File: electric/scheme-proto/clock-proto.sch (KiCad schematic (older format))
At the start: 134 parts, among them K1 servo, K2 1-wire, P1 batt, P10 led, P11 p2, P12 btn-4, P13 led, P14 led, P15 btn-5, P2 speaker, P3 dist, P4 btn-1, P5 btn-2, P6 btn-3, P7 led, P8 p1, P9 p3, Q1 bc857, Q10 bc847, Q11 bc847, Q12 bc857, Q13 bc857, Q14 bc847, Q15 bc847, Q16 bc847, Q17 bc857, Q18 bc857, Q2 bc847, Q3 bc857, Q4 bc847, Q5 irlml2244, Q6 bc847, Q7 bc857, Q8 bc847, Q9 bc857, U1 3310-LCD, U2 AD8607_2, U3 SD, U4 MINI-USB-B, U5 AD8607_2, U6 NCP3063, U7 NCP3063, U8 DS18S20

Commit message: Designing the circuit.
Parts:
- added unit 2 of U5
- U1: footprint (none) -> ~
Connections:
- net labels added: amp-vdd, nc1, nc2
- net labels removed: nc
- wire segments 431 -> 439
- no-connect marks 33 -> 34
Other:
- note added: "This is unused OpAmp part."
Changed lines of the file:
@@
 Sheet 1 1
 Title ""
-Date "18 feb 2014"
+Date "21 feb 2014"
 Rev ""
 Comp ""
@@
 	8700 3750 8700 4600
 Connection ~ 8700 4600
-Wire Wire Line
-	9800 6500 9800 6700
 $Comp
 L GND #PWR07
@@
 	1    0    0    -1
 $EndComp
-Wire Wire Line
-	8550 7100 8550 7300
 $Comp
 L GND #PWR09
@@
 Wire Wire Line
 	8900 7200 8550 7200
-Connection ~ 8550 7200
 Connection ~ 6300 13050
 Wire Wire Line
@@
 	20100 20250 20400 20250
 Wire Wire Line
-	19300 20350 19300 20550
+	19300 20200 19300 20550
 Wire Wire Line
 	20150 22200 20150 22450
@@
 $EndComp
 $Comp
-L 3310-LCD U1
-U 1 1 5301199A
-P 2150 20550
-F 0 "U1" H 2100 20650 60  0000 C CNN
-F 1 "3310-LCD" H 2050 20500 60  0000 C CNN
-F 2 "" H 2150 20550 60  0001 C CNN
-F 3 "" H 2150 20550 60  0001 C CNN
-	1    2150 20550
-	1    0    0    -1
-$EndComp
-$Comp
 L GND #PWR028
 U 1 1 53011AB9
@@
 gnd
 Text Label 28600 17600 0    60   ~ 0
-nc
+nc1
 Text Label 28600 17700 0    60   ~ 0
 3v3
@@
 gnd
 Text Label 31000 17600 0    60   ~ 0
-nc
+nc2
 Text Label 31000 17700 0    60   ~ 0
 5v
@@
 NoConn ~ 31250 17800
 $Comp
-L PWR_FLAG #FLG?
+L PWR_FLAG #FLG080
 U 1 1 5304928D
 P 8950 16500
-F 0 "#FLG?" H 8950 16595 30  0001 C CNN
+F 0 "#FLG080" H 8950 16595 30  0001 C CNN
 F 1 "PWR_FLAG" H 8950 16680 30  0000 C CNN
 F 2 "" H 8950 16500 60  0000 C CNN
@@
 	8950 16500 8950 16650
 Connection ~ 8950 16650
+$Comp
+L 3310-LCD U1
+U 1 1 5306E2C6
+P 2150 20550
+F 0 "U1" H 2100 20650 60  0000 C CNN
+F 1 "3310-LCD" H 2050 20500 60  0000 C CNN
+F 2 "~" H 2150 20550 60  0000 C CNN
+F 3 "~" H 2150 20550 60  0000 C CNN
+	1    2150 20550
+	1    0    0    -1
+$EndComp
+$Comp
+L PWR_FLAG #FLG081
+U 1 1 5306E441
+P 19300 20200
+F 0 "#FLG081" H 19300 20295 30  0001 C CNN
+F 1 "PWR_FLAG" H 19300 20380 30  0000 C CNN
+F 2 "" H 19300 20200 60  0000 C CNN
+F 3 "" H 19300 20200 60  0000 C CNN
+	1    19300 20200
+	1    0    0    -1
+$EndComp
+Wire Wire Line
+	8550 7100 8550 7300
+Connection ~ 8550 7200
+Wire Wire Line
+	9800 6700 9800 6500
+$Comp
+L PWR_FLAG #FLG082
+U 1 1 5306FE63
+P 10050 6400
+F 0 "#FLG082" H 10050 6495 30  0001 C CNN
+F 1 "PWR_FLAG" H 10050 6580 30  0000 C CNN
+F 2 "" H 10050 6400 60  0000 C CNN
+F 3 "" H 10050 6400 60  0000 C CNN
+	1    10050 6400
+	1    0    0    -1
+$EndComp
+Wire Wire Line
+	10050 6400 10050 6600
+Wire Wire Line
+	10050 6600 9800 6600
+Connection ~ 9800 6600
+$Comp
+L AD8607_2 U5
+U 2 1 530703A8
+P 15850 8500
+F 0 "U5" H 15650 8450 30  0000 C CNN
+F 1 "AD8607_2" H 15650 8550 30  0000 C CNN
+F 2 "~" H 15950 8500 60  0000 C CNN
+F 3 "~" H 15950 8500 60  0000 C CNN
+	2    15850 8500
+	1    0    0    -1
+$EndComp
+Wire Wire Line
+	14550 8300 15150 8300
+Text Label 16100 2750 0    60   ~ 0
+amp-vdd
+Text Label 15900 7800 0    60   ~ 0
+amp-vdd
+Wire Wire Line
+	15850 8000 15850 7800
+Wire Wire Line
+	15850 7800 16350 7800
+Wire Wire Line
+	15850 9000 15850 9200
+$Comp
+L GND #PWR083
+U 1 1 53070C1B
+P 15850 9200
+F 0 "#PWR083" H 15850 9200 30  0001 C CNN
+F 1 "GND" H 15850 9130 30  0001 C CNN
+F 2 "" H 15850 9200 60  0000 C CNN
+F 3 "" H 15850 9200 60  0000 C CNN
+	1    15850 9200
+	1    0    0    -1
+$EndComp
+Wire Wire Line
+	15150 8700 15000 8700
+Wire Wire Line
+	15000 8700 15000 8850
+$Comp
+L GND #PWR084
+U 1 1 53071110
+P 15000 8850
+F 0 "#PWR084" H 15000 8850 30  0001 C CNN
+F 1 "GND" H 15000 8780 30  0001 C CNN
+F 2 "" H 15000 8850 60  0000 C CNN
+F 3 "" H 15000 8850 60  0000 C CNN
+	1    15000 8850
+	1    0    0    -1
+$EndComp
+Text Label 14600 8300 0    60   ~ 0
+amp-vdd
+Text Notes 14400 7950 0    60   ~ 0
+This is unused OpAmp part.
+NoConn ~ 16550 8500
 $EndSCHEMATC

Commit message: Placing elements...
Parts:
- C8: value 4u7 -> 100n
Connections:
- net labels removed: amp-vdd
- wire segments 439 -> 438
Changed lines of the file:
@@
 Sheet 1 1
 Title ""
-Date "21 feb 2014"
+Date "22 feb 2014"
 Rev ""
 Comp ""
@@
 Wire Wire Line
 	8550 6300 8550 6700
-$Comp
-L C C8
-U 1 1 52FFCDCA
-P 8900 6900
-F 0 "C8" H 8900 7000 40  0000 L CNN
-F 1 "4u7" H 8906 6815 40  0000 L CNN
-F 2 "~" H 8938 6750 30  0000 C CNN
-F 3 "~" H 8900 6900 60  0000 C CNN
-	1    8900 6900
-	1    0    0    -1
-$EndComp
-Wire Wire Line
-	8900 6700 8900 6600
-Wire Wire Line
-	8900 6600 8550 6600
-Connection ~ 8550 6600
-Wire Wire Line
-	8900 7100 8900 7200
-Wire Wire Line
-	8900 7200 8550 7200
 Connection ~ 6300 13050
 Wire Wire Line
@@
 Text Label 31000 17600 0    60   ~ 0
 nc2
-Text Label 31000 17700 0    60   ~ 0
-5v
 Text Label 31000 17800 0    60   ~ 0
 pb9
@@
 Text Notes 15200 6450 0    60   ~ 0
 This resistances ratio \nconverts 3.3V to 5V range.
-Wire Wire Line
-	15850 4500 15850 2750
-Connection ~ 15850 2750
 $Comp
 L C C13
@@
 Wire Wire Line
 	8550 7100 8550 7300
-Connection ~ 8550 7200
 Wire Wire Line
 	9800 6700 9800 6500
@@
 Wire Wire Line
 	14550 8300 15150 8300
-Text Label 16100 2750 0    60   ~ 0
-amp-vdd
-Text Label 15900 7800 0    60   ~ 0
-amp-vdd
 Wire Wire Line
 	15850 8000 15850 7800
@@
 	1    0    0    -1
 $EndComp
-Text Label 14600 8300 0    60   ~ 0
-amp-vdd
 Text Notes 14400 7950 0    60   ~ 0
 This is unused OpAmp part.
 NoConn ~ 16550 8500
+Text Label 15900 7800 0    60   ~ 0
+filter-vdd
+Text Label 15950 3550 0    60   ~ 0
+filter-vdd
+Wire Wire Line
+	15850 3550 15850 4500
+Wire Wire Line
+	15850 3550 16850 3550
+$Comp
+L C C8
+U 1 1 5308DBDC
+P 16650 3950
+F 0 "C8" H 16650 4050 40  0000 L CNN
+F 1 "100n" H 16656 3865 40  0000 L CNN
+F 2 "~" H 16688 3800 30  0000 C CNN
+F 3 "~" H 16650 3950 60  0000 C CNN
+	1    16650 3950
+	1    0    0    -1
+$EndComp
+$Comp
+L GND #PWR085
+U 1 1 5308DBE2
+P 16650 4350
+F 0 "#PWR085" H 16650 4350 30  0001 C CNN
+F 1 "GND" H 16650 4280 30  0001 C CNN
+F 2 "" H 16650 4350 60  0000 C CNN
+F 3 "" H 16650 4350 60  0000 C CNN
+	1    16650 4350
+	1    0    0    -1
+$EndComp
+Wire Wire Line
+	16650 4150 16650 4350
+Wire Wire Line
+	16650 3750 16650 3550
+Connection ~ 16650 3550
+Text Label 14650 8300 0    60   ~ 0
+filter-vdd
 $EndSCHEMATC

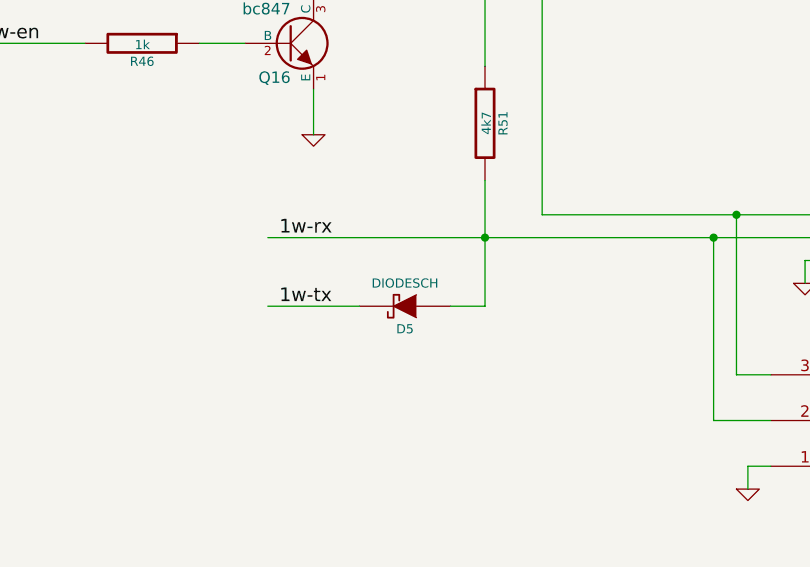
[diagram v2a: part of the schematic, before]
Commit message: Components list without unnecessary ones.
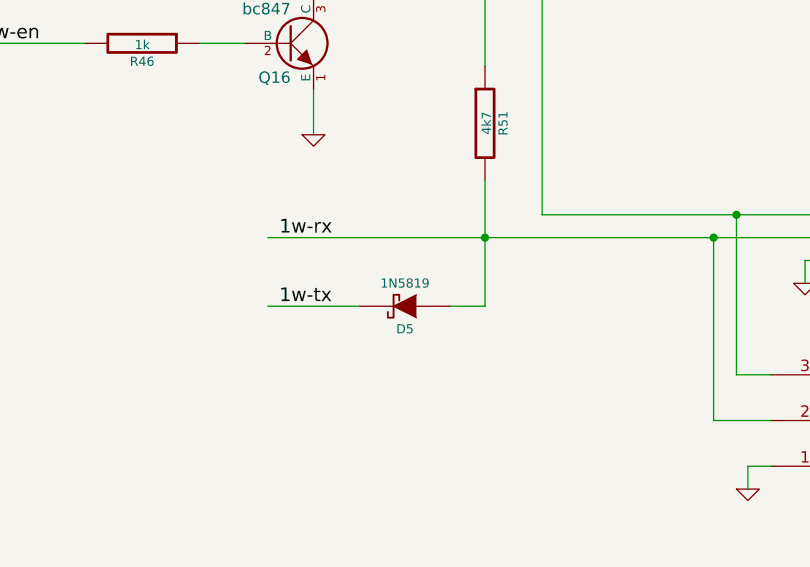
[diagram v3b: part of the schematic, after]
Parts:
- D5: value DIODESCH -> 1N5819
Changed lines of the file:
@@
 Sheet 1 1
 Title ""
-Date "22 feb 2014"
+Date "3 mar 2014"
 Rev ""
 Comp ""
@@
 P 28800 7350
 F 0 "D5" H 28800 7450 40  0000 C CNN
-F 1 "DIODESCH" H 28800 7250 40  0000 C CNN
+F 1 "1N5819" H 28800 7250 40  0000 C CNN
 F 2 "~" H 28800 7350 60  0000 C CNN
 F 3 "~" H 28800 7350 60  0000 C CNN

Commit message: Radically simplified audio scheme.
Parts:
- removed C10, C6, C9: 10n, ~, symbol C
- removed C20: 54u, ~, symbol CP1
- removed C21: 4u7, ~, symbol C
- removed C4: 1n, ~, symbol C
- removed C7, C8: 100n, ~, symbol C
- removed Q10, Q14: bc847, ~, symbol NPN
- removed Q13: bc857, ~, symbol PNP
- removed R10, R13, R18, R19, R24, R35, R37, R39, R40: 1k, ~, symbol R
- removed R16, R23, R30: 10k, ~, symbol R
- removed R17: 16k, ~, symbol R
- removed R21, R22: 2k, ~, symbol R
- removed R32: 5k1, ~, symbol R
- removed U2, U5: AD8607_2, ~, symbol AD8607_2
- added C4: 54u, ~, symbol CP1
- added D6, D7: 1N5819, symbol DIODESCH
- C5: value 10n -> 4u7
- R9: value 10k -> 100
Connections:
- net labels removed: filter-vdd, snd-amp-in
- wire segments 438 -> 364
- no-connect marks 34 -> 33
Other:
- note removed: "This is unused OpAmp part."
- note removed: "This resistances ratio \nconverts 3.3V to 5V range."
- moved on the sheet: C13, C14, Q8, Q9, R26, R27, R28, R29, R5, R6

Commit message: Remade amplifier scheme and rerouted the whole scheme respectively.
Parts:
- removed D6, D7: 1N5819, symbol DIODESCH
- added C6: 4n, ~, symbol C
- added C7, C9: 1n, ~, symbol C
- added C8: 68n, ~, symbol C
- added Q10: bc857, ~, symbol PNP
- added Q13: bc847, ~, symbol NPN
- added R10, R22: 10k, ~, symbol R
- added R13: 20k, ~, symbol R
- added R16, R18: 2k7, ~, symbol R
- added R17: 1k3, ~, symbol R
- added R19: 15k, ~, symbol R
- added R21: 1k8, ~, symbol R
- added R23, R24: 3k, ~, symbol R
- added U2: AD8607_2, ~, symbol AD8607_2
- C4: value 54u -> 47u
- R9: value 100 -> 20k
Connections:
- net labels added: opamp-vcc, ref_3v3, ref_5v
- wire segments 364 -> 414
- no-connect marks 33 -> 35
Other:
- moved on the sheet: C13, C14, C4, C5, P2, Q6, Q7, Q8, Q9, R26, R27, R28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

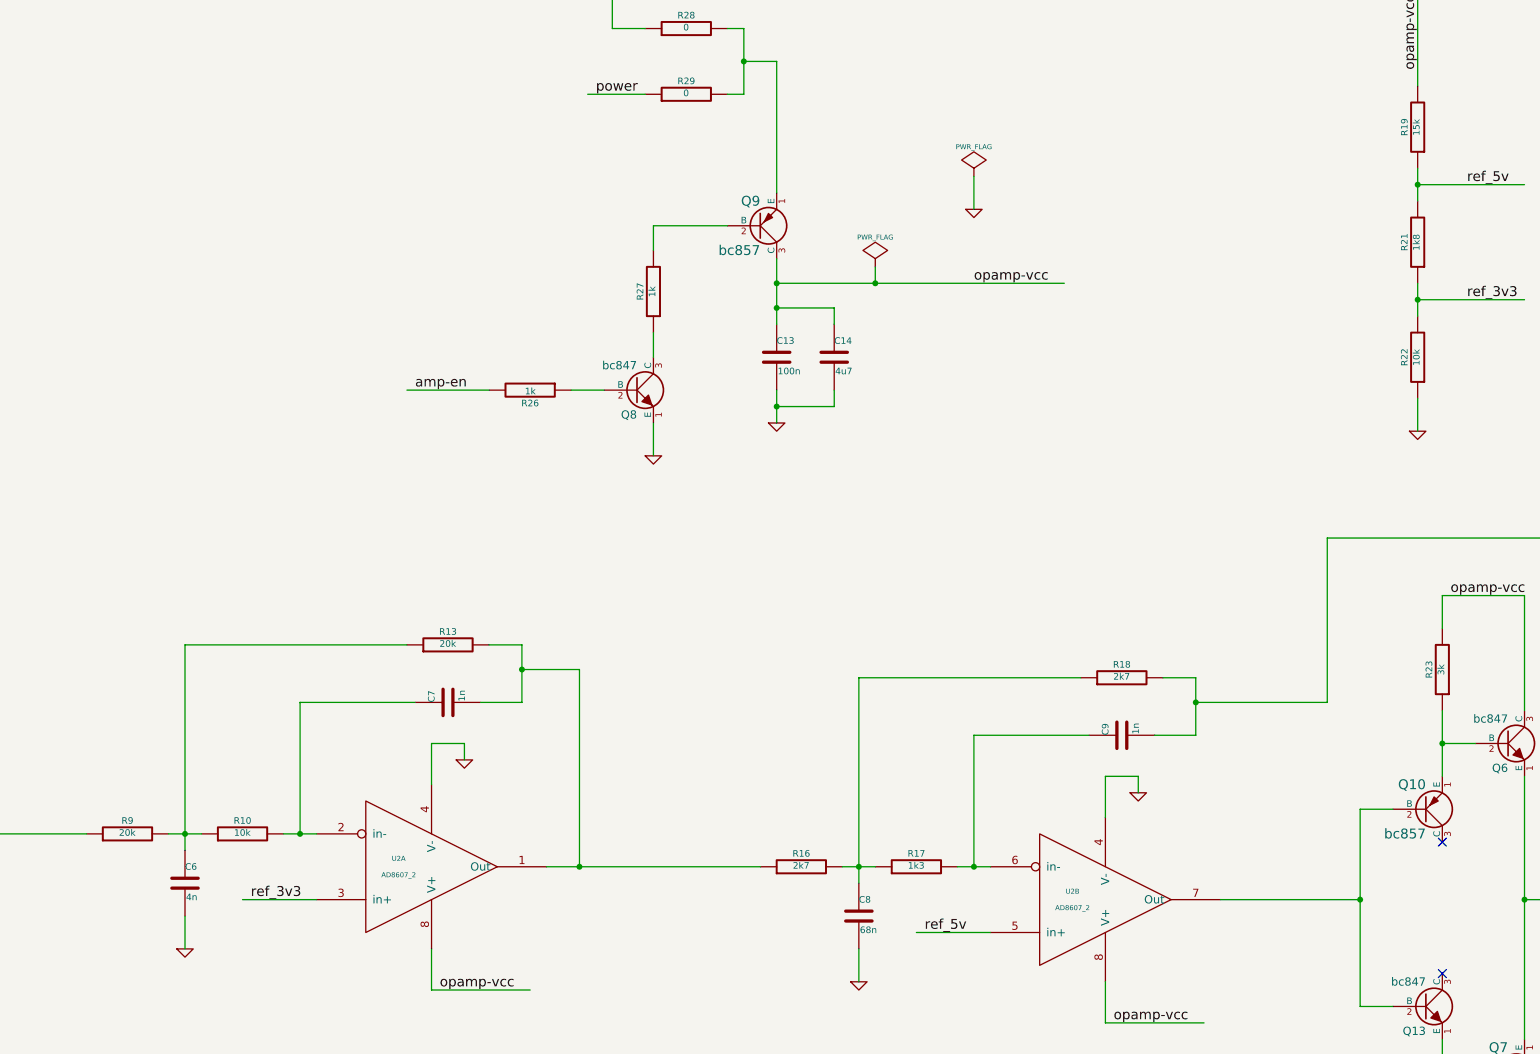
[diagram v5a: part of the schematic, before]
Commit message: Recalculated values for 12kHz low pass filter.
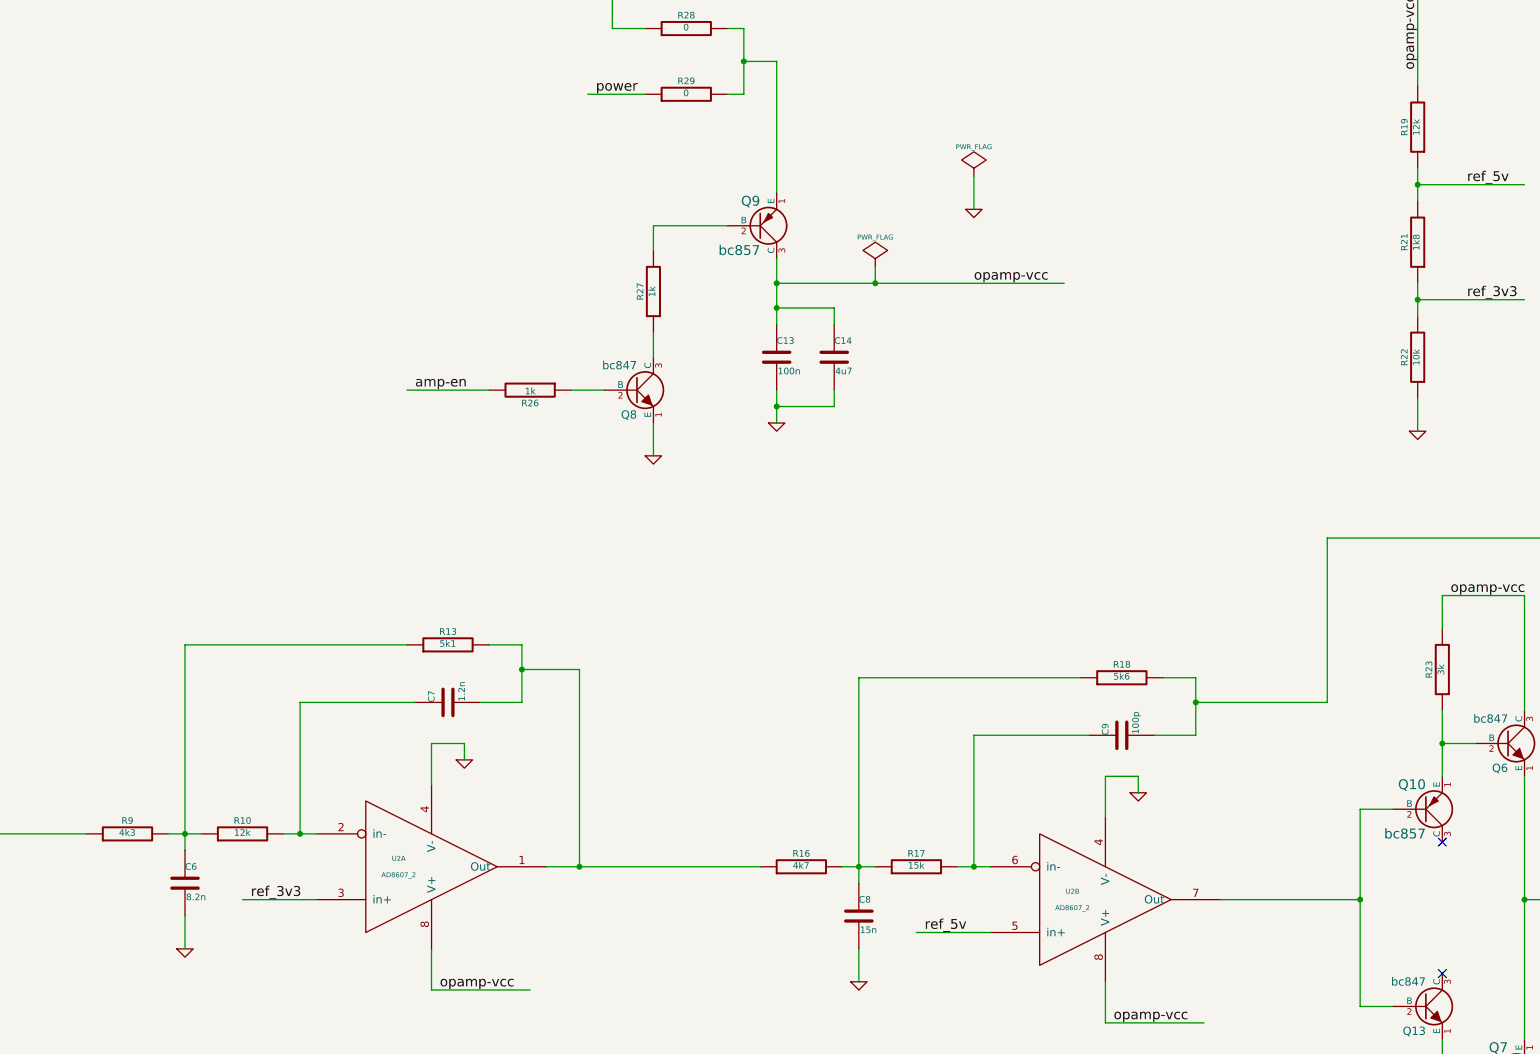
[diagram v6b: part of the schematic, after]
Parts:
- C6: value 4n -> 8.2n
- C7: value 1n -> 1.2n
- C8: value 68n -> 15n
- C9: value 1n -> 100p
- R10: value 10k -> 12k
- R13: value 20k -> 5k1
- R16: value 2k7 -> 4k7
- R17: value 1k3 -> 15k
- R18: value 2k7 -> 5k6
- R19: value 15k -> 12k
- R9: value 20k -> 4k3
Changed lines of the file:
@@
 P 4950 6550
 F 0 "R10" V 5030 6550 40  0000 C CNN
-F 1 "10k" V 4957 6551 40  0000 C CNN
+F 1 "12k" V 4957 6551 40  0000 C CNN
 F 2 "~" V 4880 6550 30  0000 C CNN
 F 3 "~" H 4950 6550 30  0000 C CNN
@@
 P 4250 6550
 F 0 "R9" V 4330 6550 40  0000 C CNN
-F 1 "20k" V 4257 6551 40  0000 C CNN
+F 1 "4k3" V 4257 6551 40  0000 C CNN
 F 2 "~" V 4180 6550 30  0000 C CNN
 F 3 "~" H 4250 6550 30  0000 C CNN
@@
 P 4600 6850
 F 0 "C6" H 4600 6950 40  0000 L CNN
-F 1 "4n" H 4606 6765 40  0000 L CNN
+F 1 "8.2n" H 4606 6765 40  0000 L CNN
 F 2 "~" H 4638 6700 30  0000 C CNN
 F 3 "~" H 4600 6850 60  0000 C CNN
@@
 P 6200 5750
 F 0 "C7" H 6200 5850 40  0000 L CNN
-F 1 "1n" H 6206 5665 40  0000 L CNN
+F 1 "1.2n" H 6206 5665 40  0000 L CNN
 F 2 "~" H 6238 5600 30  0000 C CNN
 F 3 "~" H 6200 5750 60  0000 C CNN
@@
 P 6200 5400
 F 0 "R13" V 6280 5400 40  0000 C CNN
-F 1 "20k" V 6207 5401 40  0000 C CNN
+F 1 "5k1" V 6207 5401 40  0000 C CNN
 F 2 "~" V 6130 5400 30  0000 C CNN
 F 3 "~" H 6200 5400 30  0000 C CNN
@@
 P 9050 6750
 F 0 "R17" V 9130 6750 40  0000 C CNN
-F 1 "1k3" V 9057 6751 40  0000 C CNN
+F 1 "15k" V 9057 6751 40  0000 C CNN
 F 2 "~" V 8980 6750 30  0000 C CNN
 F 3 "~" H 9050 6750 30  0000 C CNN
@@
 P 8350 6750
 F 0 "R16" V 8430 6750 40  0000 C CNN
-F 1 "2k7" V 8357 6751 40  0000 C CNN
+F 1 "4k7" V 8357 6751 40  0000 C CNN
 F 2 "~" V 8280 6750 30  0000 C CNN
 F 3 "~" H 8350 6750 30  0000 C CNN
@@
 P 8700 7050
 F 0 "C8" H 8700 7150 40  0000 L CNN
-F 1 "68n" H 8706 6965 40  0000 L CNN
+F 1 "15n" H 8706 6965 40  0000 L CNN
 F 2 "~" H 8738 6900 30  0000 C CNN
 F 3 "~" H 8700 7050 60  0000 C CNN
@@
 P 10300 5950
 F 0 "C9" H 10300 6050 40  0000 L CNN
-F 1 "1n" H 10306 5865 40  0000 L CNN
+F 1 "100p" H 10306 5865 40  0000 L CNN
 F 2 "~" H 10338 5800 30  0000 C CNN
 F 3 "~" H 10300 5950 60  0000 C CNN
@@
 P 10300 5600
 F 0 "R18" V 10380 5600 40  0000 C CNN
-F 1 "2k7" V 10307 5601 40  0000 C CNN
+F 1 "5k6" V 10307 5601 40  0000 C CNN
 F 2 "~" V 10230 5600 30  0000 C CNN
 F 3 "~" H 10300 5600 30  0000 C CNN
@@
 P 12100 2250
 F 0 "R19" V 12180 2250 40  0000 C CNN
-F 1 "15k" V 12107 2251 40  0000 C CNN
+F 1 "12k" V 12107 2251 40  0000 C CNN
 F 2 "~" V 12030 2250 30  0000 C CNN
 F 3 "~" H 12100 2250 30  0000 C CNN
